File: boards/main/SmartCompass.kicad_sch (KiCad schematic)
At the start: 20 parts, among them J1 SWD HEADER, U1 BMD-340-A-R, U2 S25FL064LABNFI043, X1 USB4085-GF-A, Y1 32.768KHZ

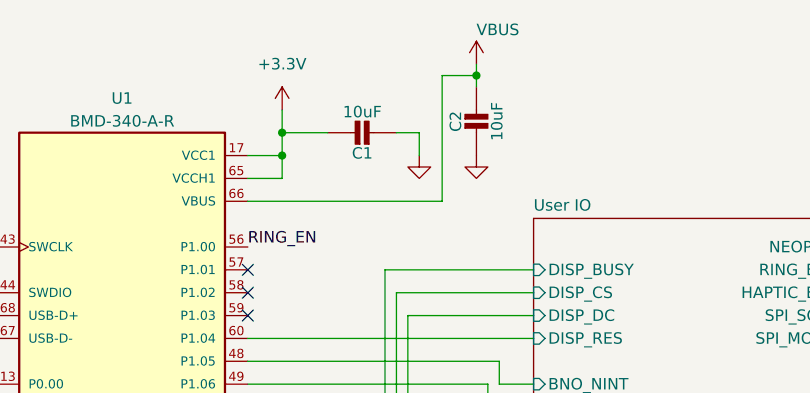
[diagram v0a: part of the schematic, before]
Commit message: Reduce the capacitance on the VBUS line to below 10uF by removing the cap by the MCU. It wasnt needed anyway
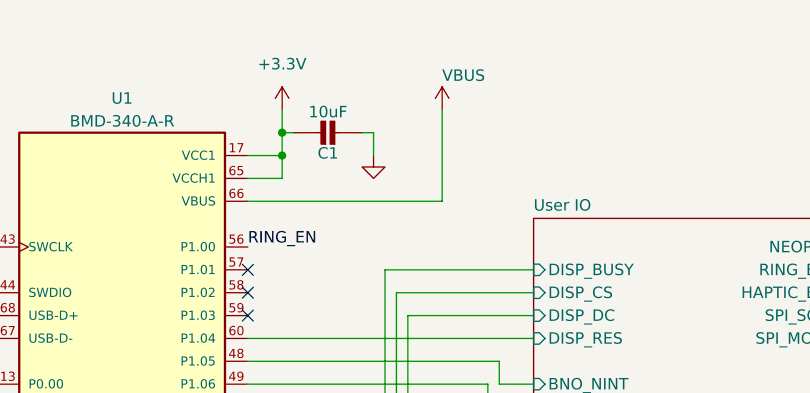
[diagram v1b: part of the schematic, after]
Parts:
- removed C2: 10uF, Capacitor_SMD:C_0805_2012Metric, symbol smart_compass_main:CAP_CERAMIC0805-NOOUTLINE
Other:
- moved on the sheet: C1
